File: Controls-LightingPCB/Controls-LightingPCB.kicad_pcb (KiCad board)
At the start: 2 copper layers, 19 parts, among them J1 Conn_01x11

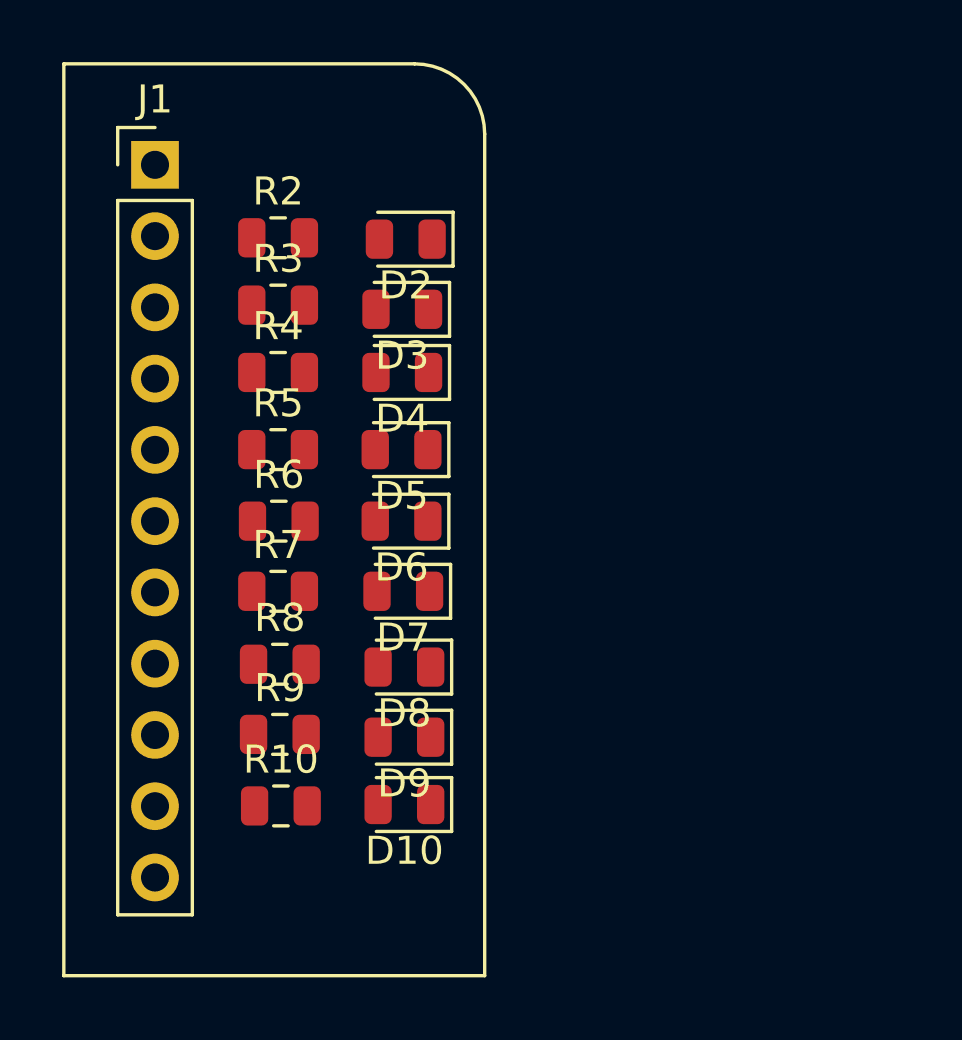
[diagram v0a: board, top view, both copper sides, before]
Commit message: Finished PCB layout
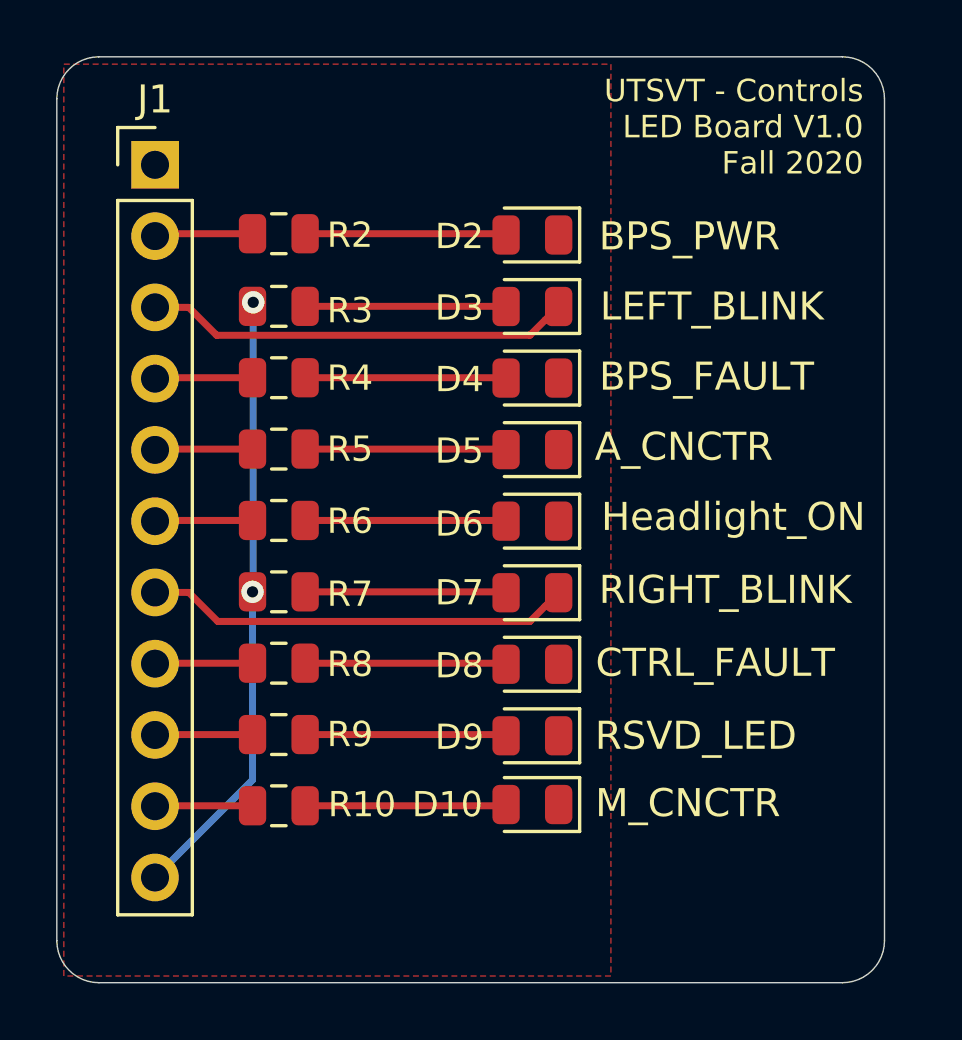
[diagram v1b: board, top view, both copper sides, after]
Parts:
- added G***: LOGO, UTSVT_Special:Hallock_Image_Small, B.Cu at (144.5, 67.8)
- added G***: LOGO, UTSVT_Special:UTSVT_Logo_Symbol, B.Cu at (136.0, 53.5)
- moved D5 4.66 mm to (141.7, 63.8)
- moved D6 4.66 mm to (141.7, 66.3)
- moved D4 4.64 mm to (141.7, 61.2)
- moved D3 4.64 mm to (141.7, 58.6)
- moved D7 4.60 mm to (141.7, 68.8)
- moved D8 4.56 mm to (141.7, 71.4)
- moved D9 4.56 mm to (141.7, 74.0)
- moved D10 4.56 mm to (141.7, 76.4)
- moved D2 4.51 mm to (141.7, 56.1)
- moved R4 0.19 mm to (132.7, 61.2)
- moved R2 0.15 mm to (132.7, 56.1)
- moved R10 0.08 mm to (132.7, 76.4)
- moved R8 0.05 mm to (132.7, 71.4)
- moved R3 0.05 mm to (132.7, 58.6)
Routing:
- net +3V3: track 0.00 -> 22.1 mm, vias 0 -> 2
- net Net-(D7-Pad1): track 0.00 -> 15.2 mm
- net Net-(D3-Pad1): track 0.00 -> 15.2 mm
- net Net-(D2-Pad2): track 0.00 -> 7.18 mm
- net Net-(D10-Pad2): track 0.00 -> 7.18 mm
- net Net-(D9-Pad2): track 0.00 -> 7.18 mm
- net Net-(D8-Pad2): track 0.00 -> 7.18 mm
- net Net-(D7-Pad2): track 0.00 -> 7.18 mm
- net Net-(D6-Pad2): track 0.00 -> 7.17 mm
- net Net-(D5-Pad2): track 0.00 -> 7.17 mm
- net Net-(D4-Pad2): track 0.00 -> 7.17 mm
- net Net-(D3-Pad2): track 0.00 -> 7.17 mm
- net Net-(J1-Pad2): track 0.00 -> 3.51 mm
- net Net-(J1-Pad4): track 0.00 -> 3.49 mm
- net Net-(J1-Pad5): track 0.00 -> 3.49 mm
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- added copper zone on F.Cu, net GNDPWR
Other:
- board outline added: 29.5 x 33 mm
- board text added: "A_CNCTR"
- board text added: "BPS_FAULT"
- board text added: "BPS_PWR"
- board text added: "CTRL_FAULT"
- board text added: "Dr. Gary Hallock"
- board text added: "Headlight_ON"
- board text added: "LEFT_BLINK"
- board text added: "M_CNCTR"
- board text added: "RIGHT_BLINK"
- board text added: "RSVD_LED"
- board text added: "UTSVT - Controls LED Board V1.0 Fall 2020"

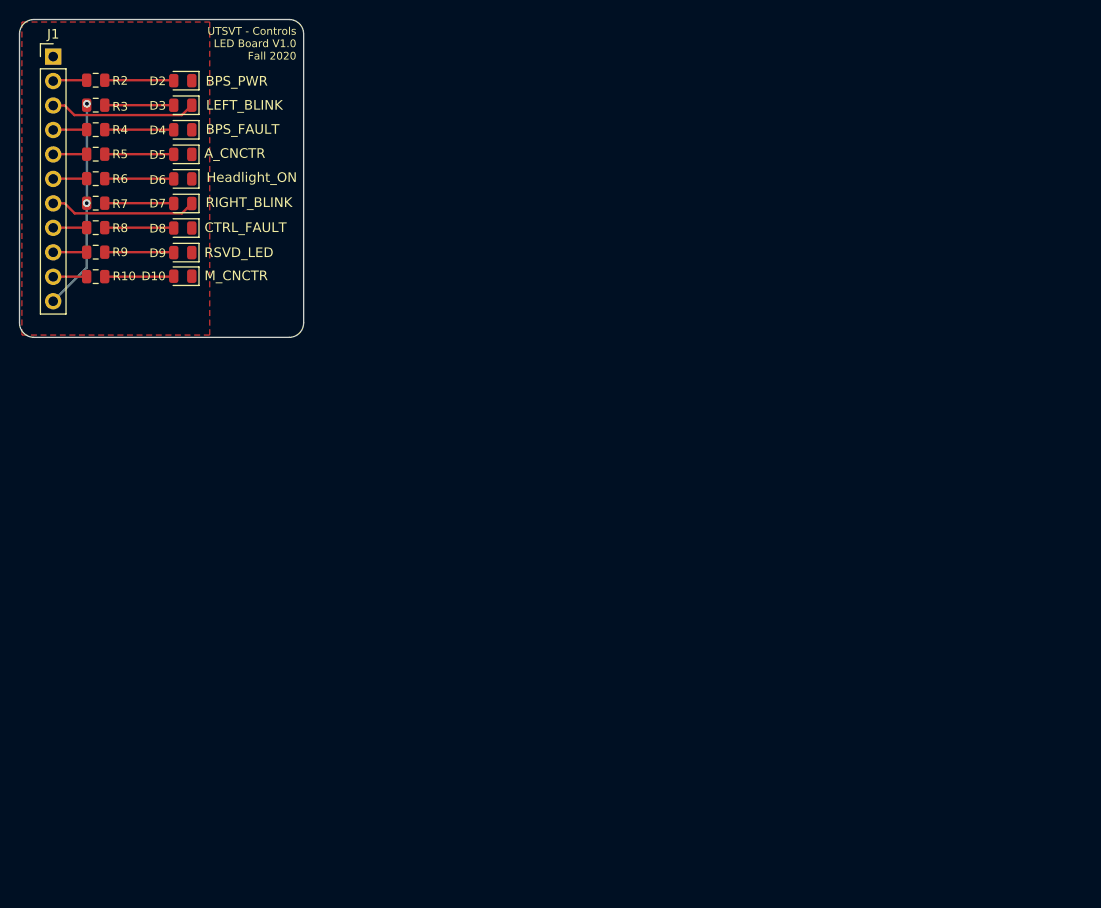
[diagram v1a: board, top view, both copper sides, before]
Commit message: Started working on PCD design, preliminary layout of components
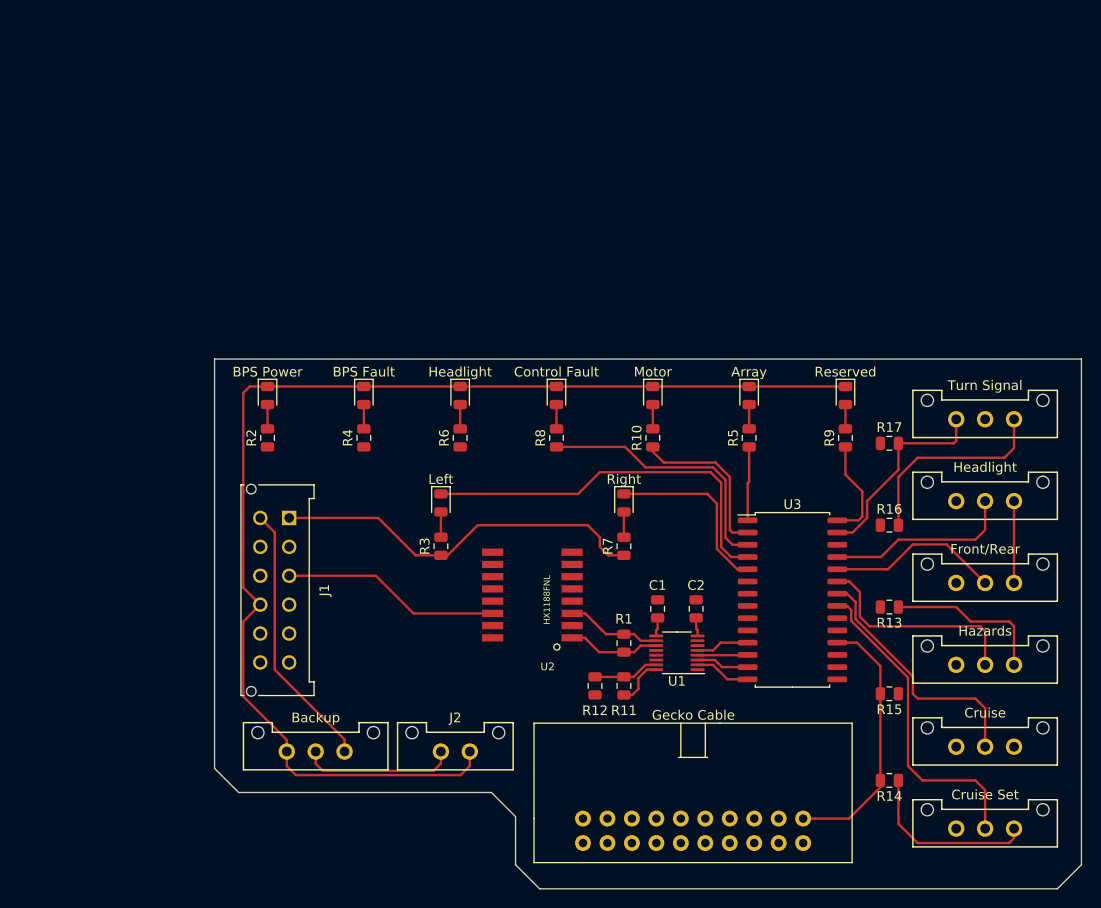
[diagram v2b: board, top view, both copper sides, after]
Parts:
- removed D10: MOTOR, Diode_SMD:D_0805_2012Metric
- removed D2: BPS_R, Diode_SMD:D_0805_2012Metric
- removed D3: LEFT, Diode_SMD:D_0805_2012Metric
- removed D4: BPS_FLT, Diode_SMD:D_0805_2012Metric
- removed D5: HLIGHTS, Diode_SMD:D_0805_2012Metric
- removed D6: RIGHT, Diode_SMD:D_0805_2012Metric
- removed D7: CTRL_FLT, Diode_SMD:D_0805_2012Metric
- removed D8: ARRAY_R, Diode_SMD:D_0805_2012Metric
- removed D9: RESERVE, Diode_SMD:D_0805_2012Metric
- removed G***: LOGO, UTSVT_Special:Hallock_Image_Small
- removed G***: LOGO, UTSVT_Special:UTSVT_Logo_Symbol
- added Array: A_CNCTR, Diode_SMD:D_0805_2012Metric, F.Cu at (200.5, 88.8)
- added BPS Fault: BPS_FAULT, Diode_SMD:D_0805_2012Metric, F.Cu at (160.5, 88.8)
- added BPS Power: BPS_PWR, Diode_SMD:D_0805_2012Metric, F.Cu at (150.5, 88.8)
- added Backup: BACKUP_SW, UTSVT_Connectors:Molex_MicroFit3.0_1x3xP3.00mm_PolarizingPeg_Vertical, F.Cu at (152.5, 125.8)
- added C1: 0.1u, Capacitor_SMD:C_0805_2012Metric, F.Cu at (191.0, 110.9)
- added C2: 0.1u, Capacitor_SMD:C_0805_2012Metric, F.Cu at (195.0, 110.9)
- added Control Fault: CTRL_FAULT, Diode_SMD:D_0805_2012Metric, F.Cu at (180.5, 88.8)
- added Cruise: CRUISE, UTSVT_Connectors:Molex_MicroFit3.0_1x3xP3.00mm_PolarizingPeg_Vertical, F.Cu at (222.0, 125.2)
- added Cruise Set: CRUISE_SET, UTSVT_Connectors:Molex_MicroFit3.0_1x3xP3.00mm_PolarizingPeg_Vertical, F.Cu at (222.0, 133.8)
- added Front/Rear: F/R_SW, UTSVT_Connectors:Molex_MicroFit3.0_1x3xP3.00mm_PolarizingPeg_Vertical, F.Cu at (222.0, 108.2)
- added Gecko Cable: Gecko_Cable, UTSVT_Connectors:ribbon_cable_right_2x10, F.Cu at (183.2, 135.2)
- added Hazards: HAZARD, UTSVT_Connectors:Molex_MicroFit3.0_1x3xP3.00mm_PolarizingPeg_Vertical, F.Cu at (222.0, 116.8)
- added Headlight: HEADLIGHT_SW, UTSVT_Connectors:Molex_MicroFit3.0_1x3xP3.00mm_PolarizingPeg_Vertical, F.Cu at (222.0, 99.8)
- added Headlight: Headlight_ON, Diode_SMD:D_0805_2012Metric, F.Cu at (170.5, 88.8)
- added J2: Backup, UTSVT_Connectors:Molex_MicroFit3.0_1x2xP3.00mm_PolarizingPeg_Vertical, F.Cu at (168.5, 125.8)
- added Left: LEFT_BLINK, Diode_SMD:D_0805_2012Metric, F.Cu at (168.5, 99.9)
- added Motor: M_CNCTR, Diode_SMD:D_0805_2012Metric, F.Cu at (190.5, 88.8)
- added R1: 120, Resistor_SMD:R_0805_2012Metric, F.Cu at (187.5, 114.5)
- added R11: 806, Resistor_SMD:R_0805_2012Metric, F.Cu at (187.5, 118.9)
- added R12: 1.2k, Resistor_SMD:R_0805_2012Metric, F.Cu at (184.5, 118.9)
- added R13: 10k, Resistor_SMD:R_0805_2012Metric, F.Cu at (215.1, 110.8)
- added R14: 10k, Resistor_SMD:R_0805_2012Metric, F.Cu at (215.1, 128.8)
- added R15: 10k, Resistor_SMD:R_0805_2012Metric, F.Cu at (215.1, 119.8)
- added R16: 10k, Resistor_SMD:R_0805_2012Metric, F.Cu at (215.1, 102.2)
- added R17: 10k, Resistor_SMD:R_0805_2012Metric, F.Cu at (215.1, 93.8)
- added Reserved: RSVD_LED, Diode_SMD:D_0805_2012Metric, F.Cu at (210.5, 88.8)
- added Right: RIGHT_BLINK, Diode_SMD:D_0805_2012Metric, F.Cu at (187.5, 99.9)
- added Turn Signal: TURN_SIGNAL_SW, UTSVT_Connectors:Molex_MicroFit3.0_1x3xP3.00mm_PolarizingPeg_Vertical, F.Cu at (222.0, 91.2)
- added U1: LTC6820, Package_SO:MSOP-16_3x4mm_P0.5mm, F.Cu at (193.0, 115.5)
- added U2: HX1188FNL, UTSVT_Passive:HXXXX, F.Cu at (178.0, 109.5)
- added U3: MCP23S17_SO, Package_SO:SOIC-28W_7.5x17.9mm_P1.27mm, F.Cu at (205.0, 110.0)
- J1: value Conn_01x11 -> MinionConn; footprint Connector_PinHeader_2.54mm:PinHeader_1x11_P2.54mm_Vertical -> UTSVT_Connectors:Molex_MicroFit3.0_2x6xP3.00mm_PolarizingPeg_Vertical
- moved R9 80.2 mm to (210.5, 93.2), turned to 90 degrees
- moved R5 74.0 mm to (200.5, 93.2), turned to 90 degrees
- moved R7 65.4 mm to (187.5, 104.4), turned to 90 degrees
- moved R10 60.2 mm to (190.5, 93.2), turned to 90 degrees
- moved R3 58.1 mm to (168.5, 104.4), turned to 90 degrees
- moved J1 53.8 mm to (152.8, 101.5), turned to 270 degrees
- moved R8 52.6 mm to (180.5, 93.2), turned to 90 degrees
- moved R6 46.4 mm to (170.5, 93.2), turned to 90 degrees
- moved R4 42.4 mm to (160.5, 93.2), turned to 90 degrees
- moved R2 41.2 mm to (150.5, 93.2), turned to 90 degrees
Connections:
- J1 pad 1: GNDPWR -> +3V3
- J1 pad 10: Net-(J1-Pad10) -> GNDPWR
- J1 pad 11: +3V3 -> Net-(J1-Pad11)
- J1 pad 4: Net-(J1-Pad4) -> GND
- J1 pad 7: Net-(D7-Pad1) -> +12V
- J1 pad 8: Net-(J1-Pad8) -> /UART-Tx
- J1 pad 9: Net-(J1-Pad9) -> /UART_Rx
- R10 pad 1: Net-(J1-Pad10) -> /ControlLEDs/M_CNCTR
- R2 pad 1: Net-(J1-Pad2) -> /ControlLEDs/BPS_PWR
- R4 pad 1: Net-(J1-Pad4) -> /ControlLEDs/BPS_FAULT
- R5 pad 1: Net-(J1-Pad5) -> /ControlLEDs/A_CNCTR
- R6 pad 1: Net-(J1-Pad6) -> /ControlLEDs/Headlight_ON
- R8 pad 1: Net-(J1-Pad8) -> /ControlLEDs/CTRL_FAULT
- R9 pad 1: Net-(J1-Pad9) -> /ControlLEDs/RSVD_LED
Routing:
- net GNDPWR: track 0.00 -> 126.1 mm
- net +3V3: track 22.1 -> 79.3 mm, vias 2 -> 0
- net /ControlLEDs/LEFT_BLINK: track 0.00 -> 40.3 mm
- net /ControlSwitches/CRUZ_ST: track 0.00 -> 33.3 mm
- net +12V: track 0.00 -> 27.9 mm
- net /ControlLEDs/CTRL_FAULT: track 0.00 -> 27.6 mm
- net /ControlSwitches/CRUZ_EN: track 0.00 -> 26.4 mm
- net /ControlSwitches/HZD_SW: track 0.00 -> 22.5 mm
- net /ControlSwitches/LEFT_SW: track 0.00 -> 21.2 mm
- net /ControlSwitches/RIGHT_SW: track 0.00 -> 21.2 mm
- net /ControlSwitches/Headlight_SW: track 0.00 -> 19.5 mm
- net /ControlLEDs/RIGHT_BLINK: track 0.00 -> 18.8 mm
- net Net-(R14-Pad1): track 0.00 -> 18.5 mm
- net /ControlSwitches/FR_SW: track 0.00 -> 18.1 mm
- net /ControlLEDs/M_CNCTR: track 0.00 -> 17.0 mm
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- removed copper zone on F.Cu, net GNDPWR
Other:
- board size 29.5 x 33 mm -> 90 x 55 mm
- board text removed: "A_CNCTR"
- board text removed: "BPS_FAULT"
- board text removed: "BPS_PWR"
- board text removed: "CTRL_FAULT"
- board text removed: "Dr. Gary Hallock"
- board text removed: "Headlight_ON"
- board text removed: "LEFT_BLINK"
- board text removed: "M_CNCTR"
- board text removed: "RIGHT_BLINK"
- board text removed: "RSVD_LED"
- board text removed: "UTSVT - Controls LED Board V1.0 Fall 2020"
